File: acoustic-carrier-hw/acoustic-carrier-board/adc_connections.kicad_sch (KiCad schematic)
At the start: 26 parts, among them IC1 ECP5-BGA256, J2 Conn_02x08_Odd_Even, U7 MS9280

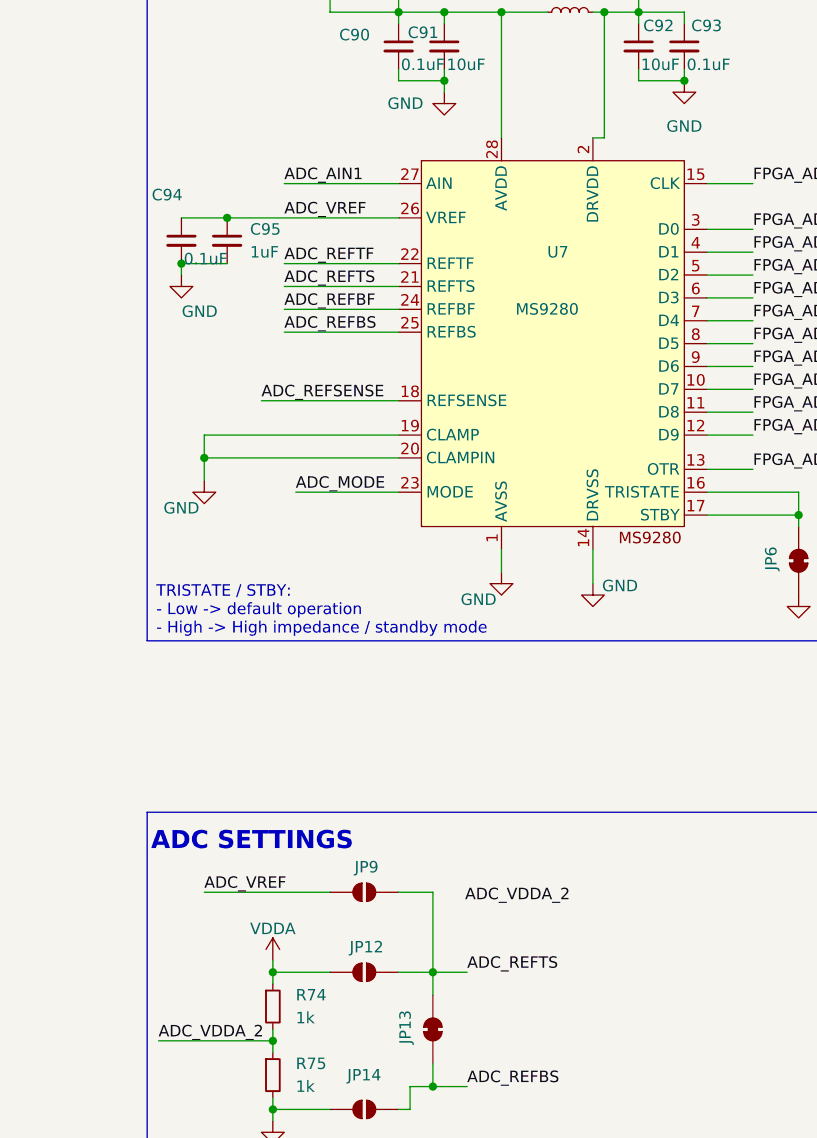
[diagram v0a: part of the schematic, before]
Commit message: [carrier] Added buffered VOCM (next) add switch on which was decided, add biasing after ac coupling caps, add provisionary pull-ups at of THS452 INPUT-
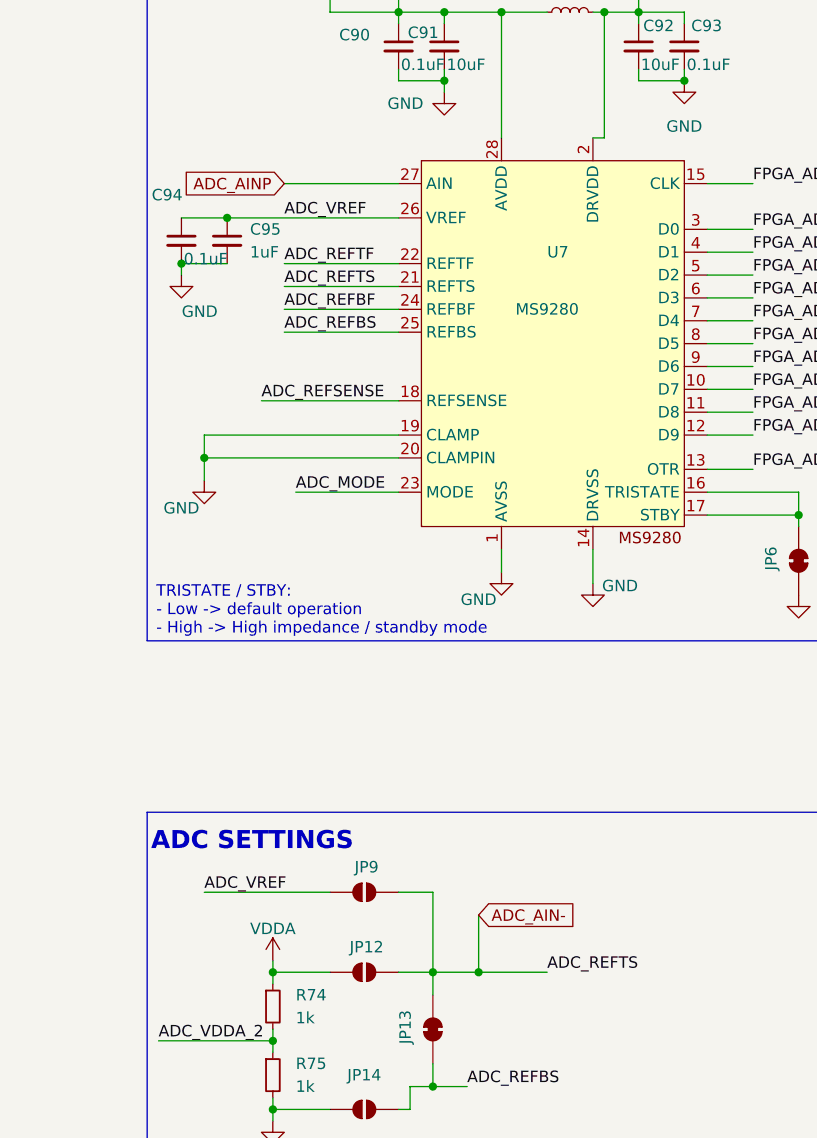
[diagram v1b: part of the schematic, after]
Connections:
- net ADC_AIN1 renamed ADC_AINP
- net ADC_REFTS renamed ADC_AIN-

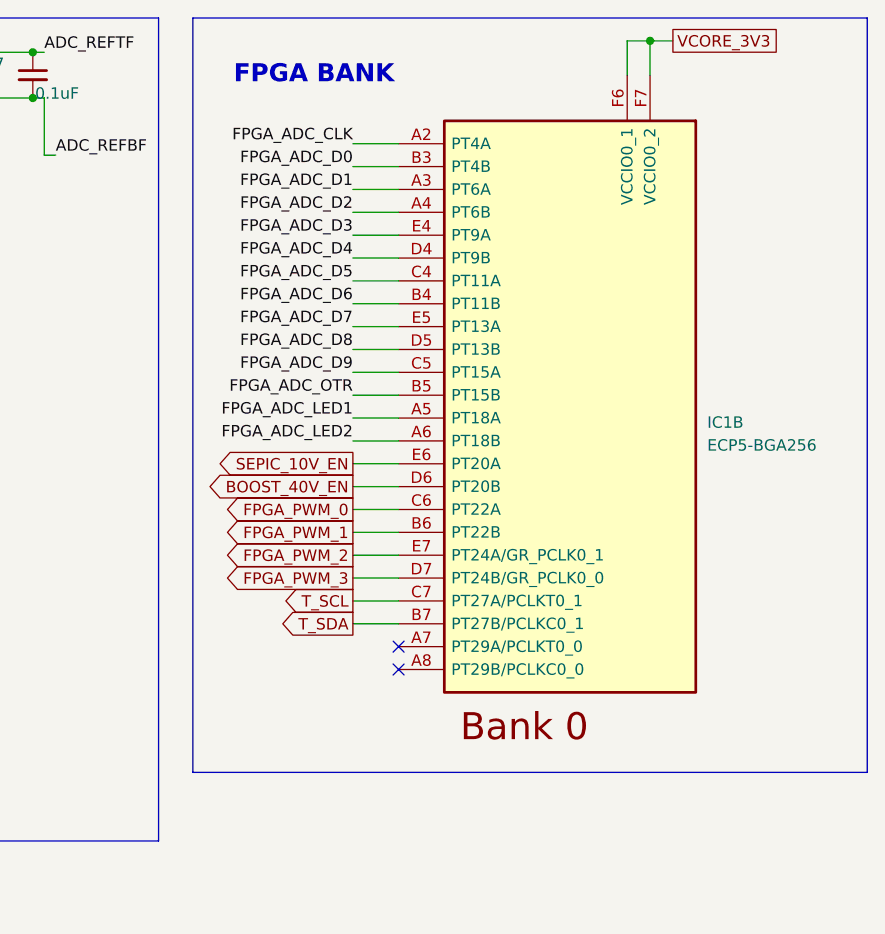
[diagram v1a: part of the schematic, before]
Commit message: [carrier] Added switch (next) add appropriate test point on secondary dpdt
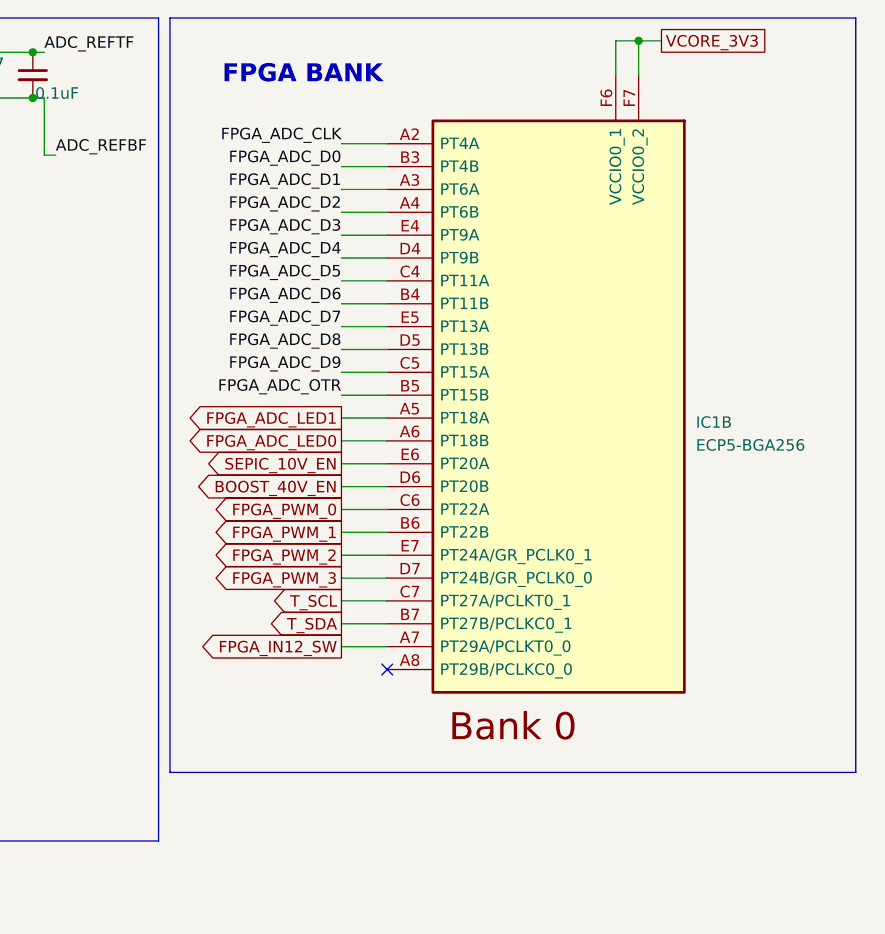
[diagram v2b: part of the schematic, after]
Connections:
- net FPGA_IN12_SW: now reaches IC1.A7 (PT29A/PCLKT0_0)
- net FPGA_ADC_LED2 renamed FPGA_ADC_LED0
- no-connect marks 2 -> 1
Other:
- moved on the sheet: IC1B

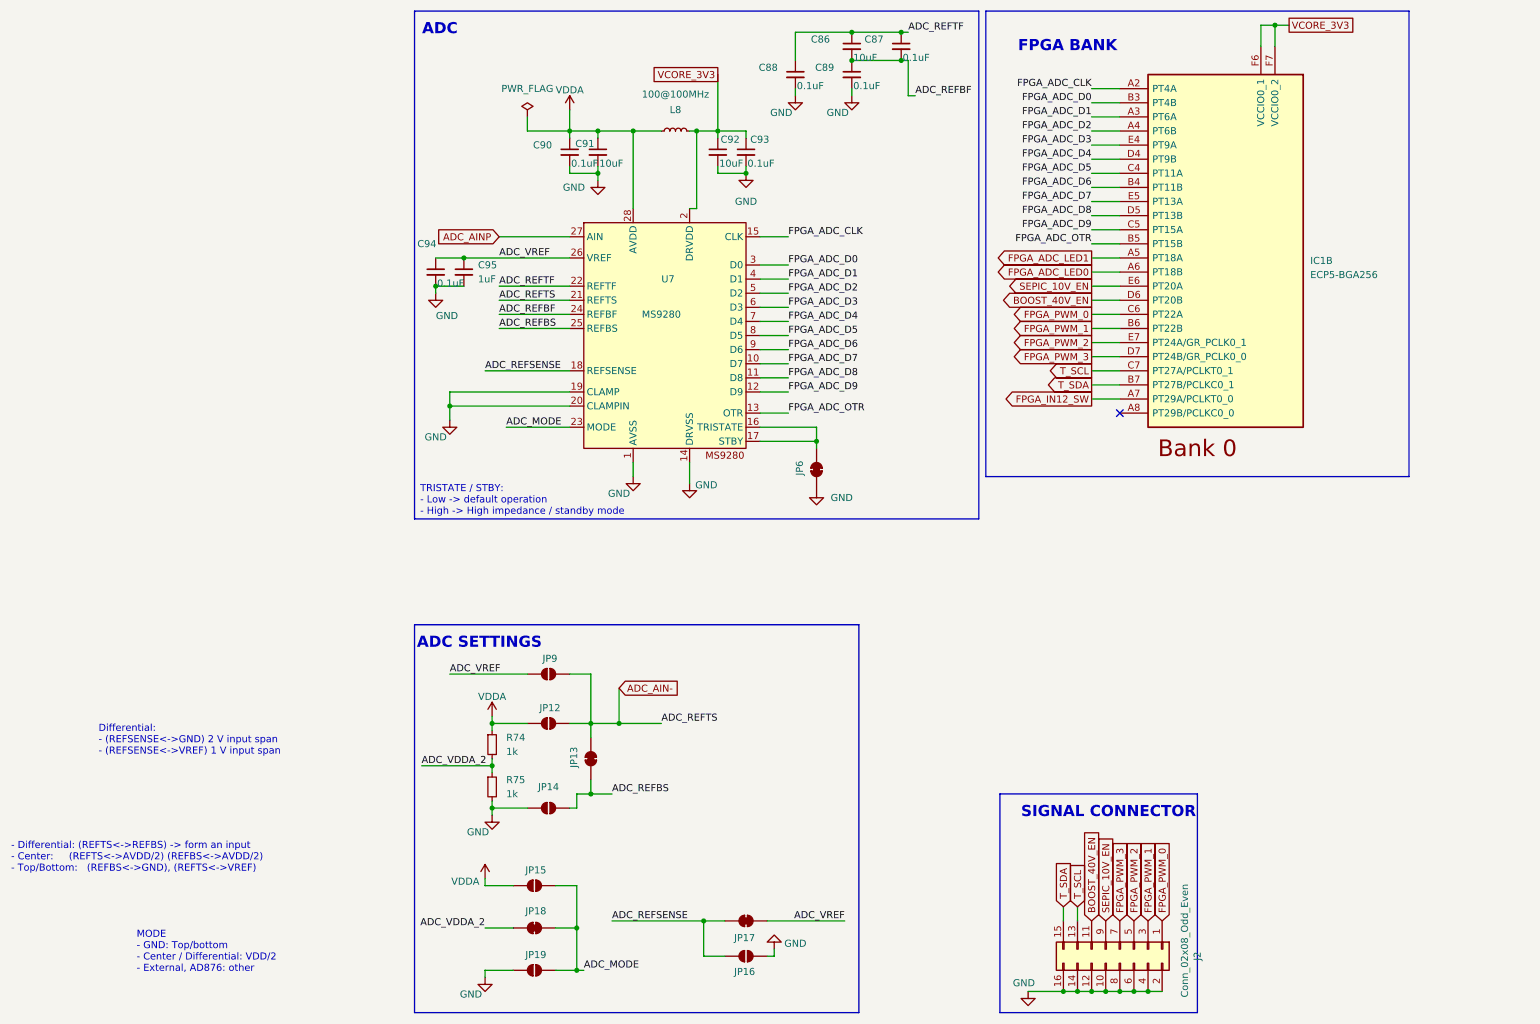
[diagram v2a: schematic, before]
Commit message: [carrier] Replaced voltage reference, added extra 0 ohm resistors, added test-connectors for ADC testing
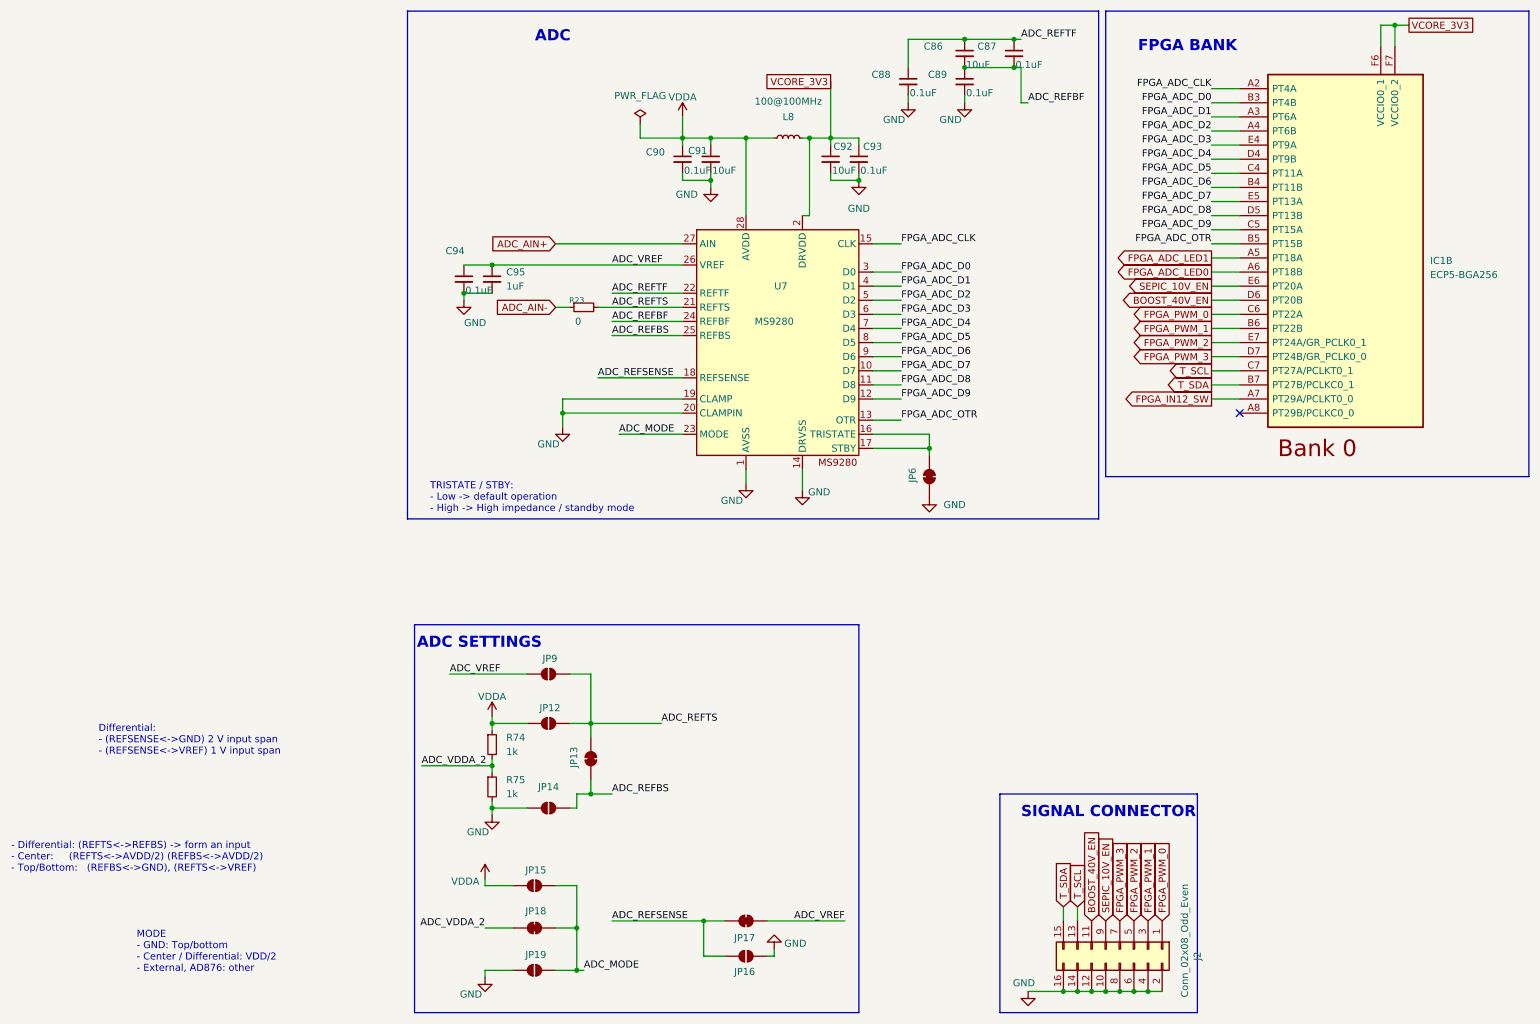
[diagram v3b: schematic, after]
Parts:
- added R23: 0, Resistor_SMD:R_0603_1608Metric, symbol Device:R_Small
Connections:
- net ADC_AIN-: now also R23.1; no longer JP12.2 (B), JP13.2 (B), JP9.2 (B), U7.21 (REFTS)
- net ADC_AINP renamed ADC_AIN+
- new net ADC_REFTS: JP12.2 (B), JP13.2 (B), JP9.2 (B), R23.2, U7.21 (REFTS)
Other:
- moved on the sheet: C86, C87, C88, C89, C90, C91, C92, C93, C94, C95, IC1B, JP6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
